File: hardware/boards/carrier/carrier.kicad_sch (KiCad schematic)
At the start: 43 parts, among them J1 XT30PW(2+2)-M.G.B_SLOT, Q1 IPB020N10N5LF, Q2 2N7002, Q3 2N7002, U2 LM5163DDAR, U3 LMX5069MS, U4 INA237AIDGSR

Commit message: hardware: standardize carrier schematic presentation
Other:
- sheet STM32 Housekeeping and Status ports: added none; removed +3V3, GND

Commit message: checkpoint: carrier schematic refinements
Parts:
- C1: value 1uF 100V X7R -> 1uF 100V
- C2: value 680nF 10% X7R -> 680nF
- J1: value XT30PW(2+2)-M.G.B_SLOT -> XT30PW(2+2)
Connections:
- net VIN_RAW: no longer J1.1 (Pin_1)
- new net VCC: J1.1 (Pin_1)
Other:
- moved on the sheet: C10, R18, R8

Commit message: hardware: split carrier power controls and adopt SMBus
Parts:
- removed C1: 1uF 100V, Capacitor_SMD:C_1206_3216Metric, symbol Device:C
- removed C10: 100nF diff, Capacitor_SMD:C_0603_1608Metric, symbol Device:C
- removed C2: 680nF, Capacitor_SMD:C_0603_1608Metric, symbol Device:C
- removed D1: SMCJ48A, Diode_SMD:D_SMC, symbol Device:D_Zener
- removed MOD1: SW3538_140W_Module, mini-rack-power:SW3538_140W_Module, symbol mini-rack-power:SW3538_140W_Module
- removed Q1: IPB020N10N5LF, Package_TO_SOT_SMD:TO-263-3_TabPin2, symbol Transistor_FET:Q_NMOS_GDS
- removed Q2, Q3: 2N7002, Package_TO_SOT_SMD:SOT-23, symbol Transistor_FET:2N7002
- removed R1: 6mR 1% 3W, Resistor_SMD:R_2512_6332Metric, symbol Device:R
- removed R10: 100k, Resistor_SMD:R_0603_1608Metric, symbol Device:R
- removed R11, R19: 10k, Resistor_SMD:R_0603_1608Metric, symbol Device:R
- removed R17, R18: 10R, Resistor_SMD:R_0603_1608Metric, symbol Device:R
- removed R2: 100R, Resistor_SMD:R_0603_1608Metric, symbol Device:R
- removed R20: 0R A0=0, Resistor_SMD:R_0603_1608Metric, symbol Device:R
- removed R21: 0R A0=1 DNP, Resistor_SMD:R_0603_1608Metric, symbol Device:R
- removed R22: 0R A1=0, Resistor_SMD:R_0603_1608Metric, symbol Device:R
- removed R23: 0R A1=1 DNP, Resistor_SMD:R_0603_1608Metric, symbol Device:R
- removed R3: 36.0k 1%, Resistor_SMD:R_0603_1608Metric, symbol Device:R
- removed R4: 110k 1% UVLO, Resistor_SMD:R_0603_1608Metric, symbol Device:R
- removed R5: 18k 1% UVLO, Resistor_SMD:R_0603_1608Metric, symbol Device:R
- removed R6: 110k 1% OVLO, Resistor_SMD:R_0603_1608Metric, symbol Device:R
- removed R7: 5.1k 1% OVLO, Resistor_SMD:R_0603_1608Metric, symbol Device:R
- removed R8: 110k 1%, Resistor_SMD:R_0603_1608Metric, symbol Device:R
- removed R9: 36k 1%, Resistor_SMD:R_0603_1608Metric, symbol Device:R
- removed U3: LMX5069MS, Package_SO:MSOP-10_3x3mm_P0.5mm, symbol Power_Management:LM5069MM-2
- removed U4: INA237AIDGSR, Package_SO:TSSOP-10_3x3mm_P0.5mm, symbol Sensor_Energy:INA237
- C3, C4: value 2.2uF 100V X7R -> 2.2uF 100V
- C5: value 2.2nF 50V X7R -> 2.2nF 50V
- C6: value 2.2nF X7R -> 2.2nF
- C7: value 220pF C0G -> 220pF
- C8: value 22uF 25V X7R -> 22uF 25V
- L1: value 68uH YNR6045-680M -> 68uH
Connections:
- net VIN_RAW is gone; now on net VCC: C3.1, C4.1, U2.2 (VIN), U2.3 (EN/UVLO)
- net UP_I2C_SCL renamed BP_SMBUS_SCL
- net UP_I2C_SDA renamed BP_SMBUS_SDA
- no-connect marks 1 -> 0
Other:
- added sheet Protected Power and Controls (01_power_control.kicad_sch)
- sheet STM32 Housekeeping and Status ports: added BP_SMBUS_SCL, BP_SMBUS_SDA; removed UP_I2C_SCL, UP_I2C_SDA
- note added: "ASSEMBLY / FOOTPRINT CHECKS L1 footprint intentionally unassigned: create/verify against the YNR6045 manufacturer land pattern. Verify U2 package pin numbering and exposed-pad requirements against manufacturer drawings."
- note added: "BACKPLANE INTERFACE + LOCAL 3.3 V SUPPLY"
- note added: "RELEASE BLOCKER - CONNECTOR POLARITY Current carrier assumption: J1 pin 1 = VCC, pin 2 = GND, pin 3 = SMBus SDA, pin 4 = SMBus SCL. Backplane-prototype presently shows the power pins oppositely. Confirm physical mated contacts and drawing viewpoints, then make symbol pins, footprint pads, net assignments, and notes consistent in every carrier/backplane project before fabrication."
- note removed: "ASSEMBLY / FOOTPRINT CHECKS L1 footprint intentionally unassigned: create/verify against the YNR6045 manufacturer land pattern. Before PCB work, verify U1/U2/U3/U4/Q1 package pin numbering and exposed-pad requirements against manufacturer drawings. R21/R23 select alternate INA237 address states and are DNP."
- note removed: "BACKPLANE INTERFACE + PROTECTED PD POWER"
- note removed: "Default OFF: R8/R9 drive Q2 on unless PA1 drives Q3. LMX5069 auto-retries; STM32 observes PD_PGOOD and may remove PD_ENABLE."
- note removed: "POWER / CURRENT MONITOR"
- note removed: "Power path: VIN_RAW -> R1 (6 mR Kelvin-routed) -> HS_SENSE -> Q1 -> PD_VIN_SW"
- note removed: "Q1 SOA RELEASE GATE Prove IPB020N10N5LF at the hot corner: approximately 66 W inferred maximum power limit and 66.5 ms maximum TIMER interval. Do not substitute Q1 using RDS(on) alone. Validate current/power limits and startup on hardware."
- note removed: "R17/R18 are Kelvin sense traces from the R1 pads. U4 VBUS intentionally measures after Q1."
- note removed: "RELEASE BLOCKER - CONNECTOR POLARITY Current carrier assumption: J1 pin 1 = VIN_RAW, pin 2 = GND, pin 3 = SDA, pin 4 = SCL. Backplane-prototype presently shows the power pins oppositely. Confirm physical mated contacts and drawing viewpoints, then make symbol pins, footprint pads, net assignments, and notes consistent in every carrier/backplane project before fabrication."
- title: USB-C PD Carrier - Protected Power and Local Supply -> USB-C PD Carrier - Backplane Interface and Local Supply

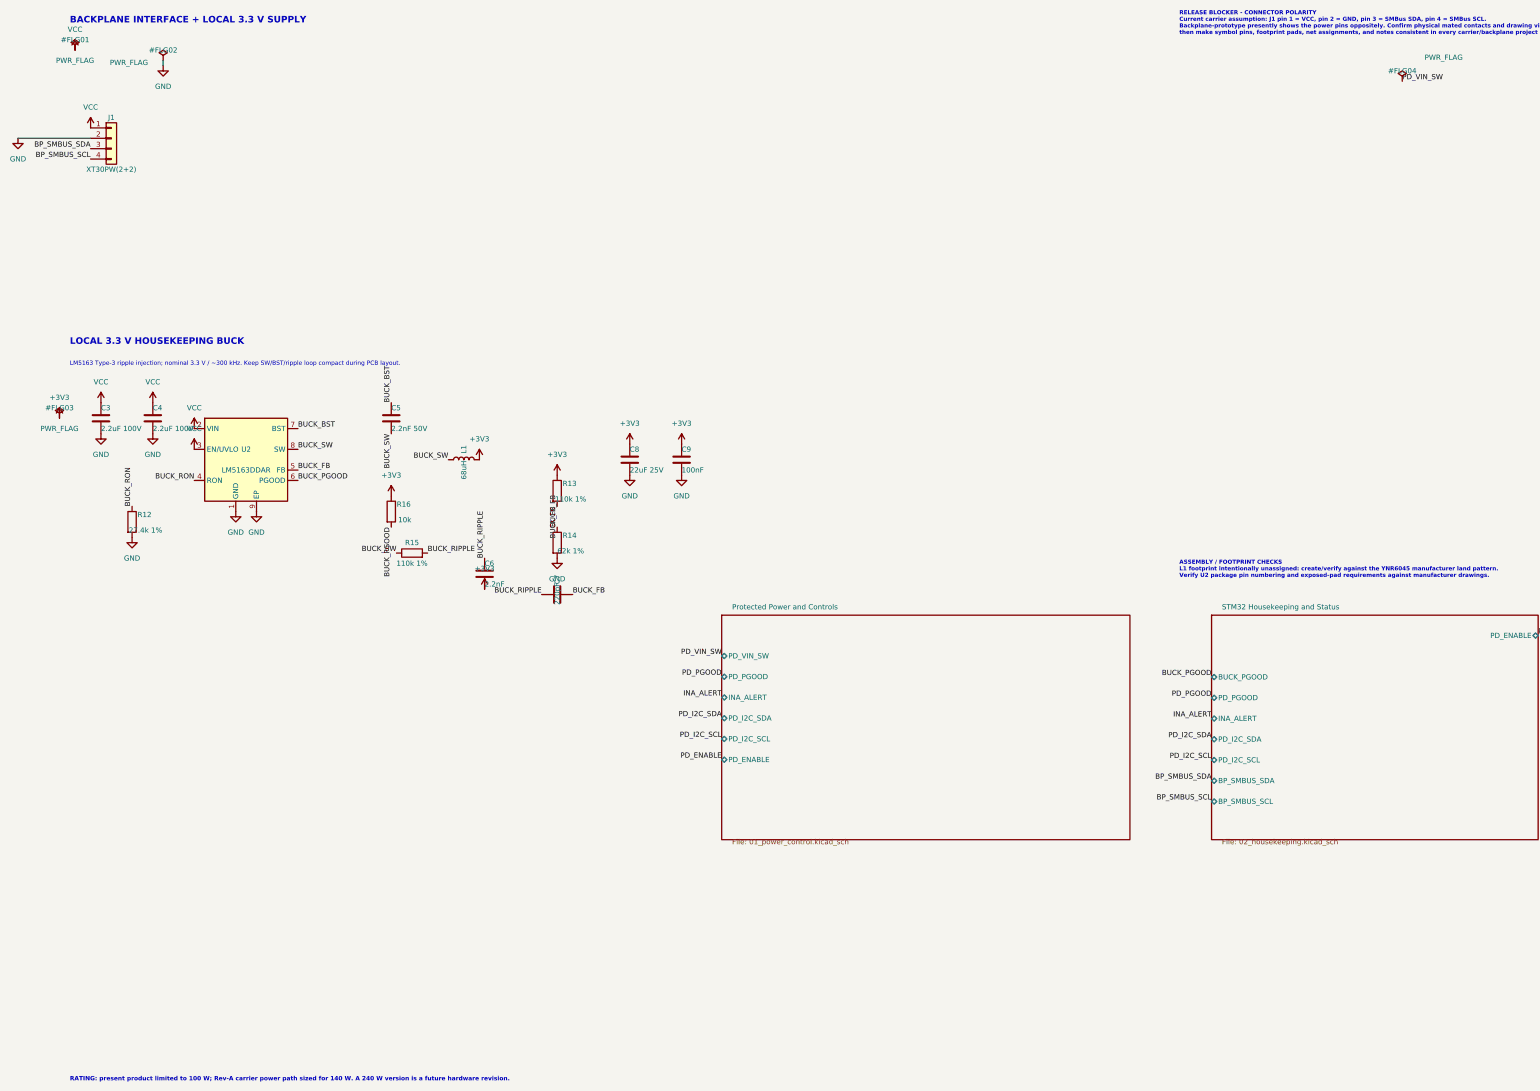
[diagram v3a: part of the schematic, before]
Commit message: checkpoint: carrier schematic edits and SW3538 references
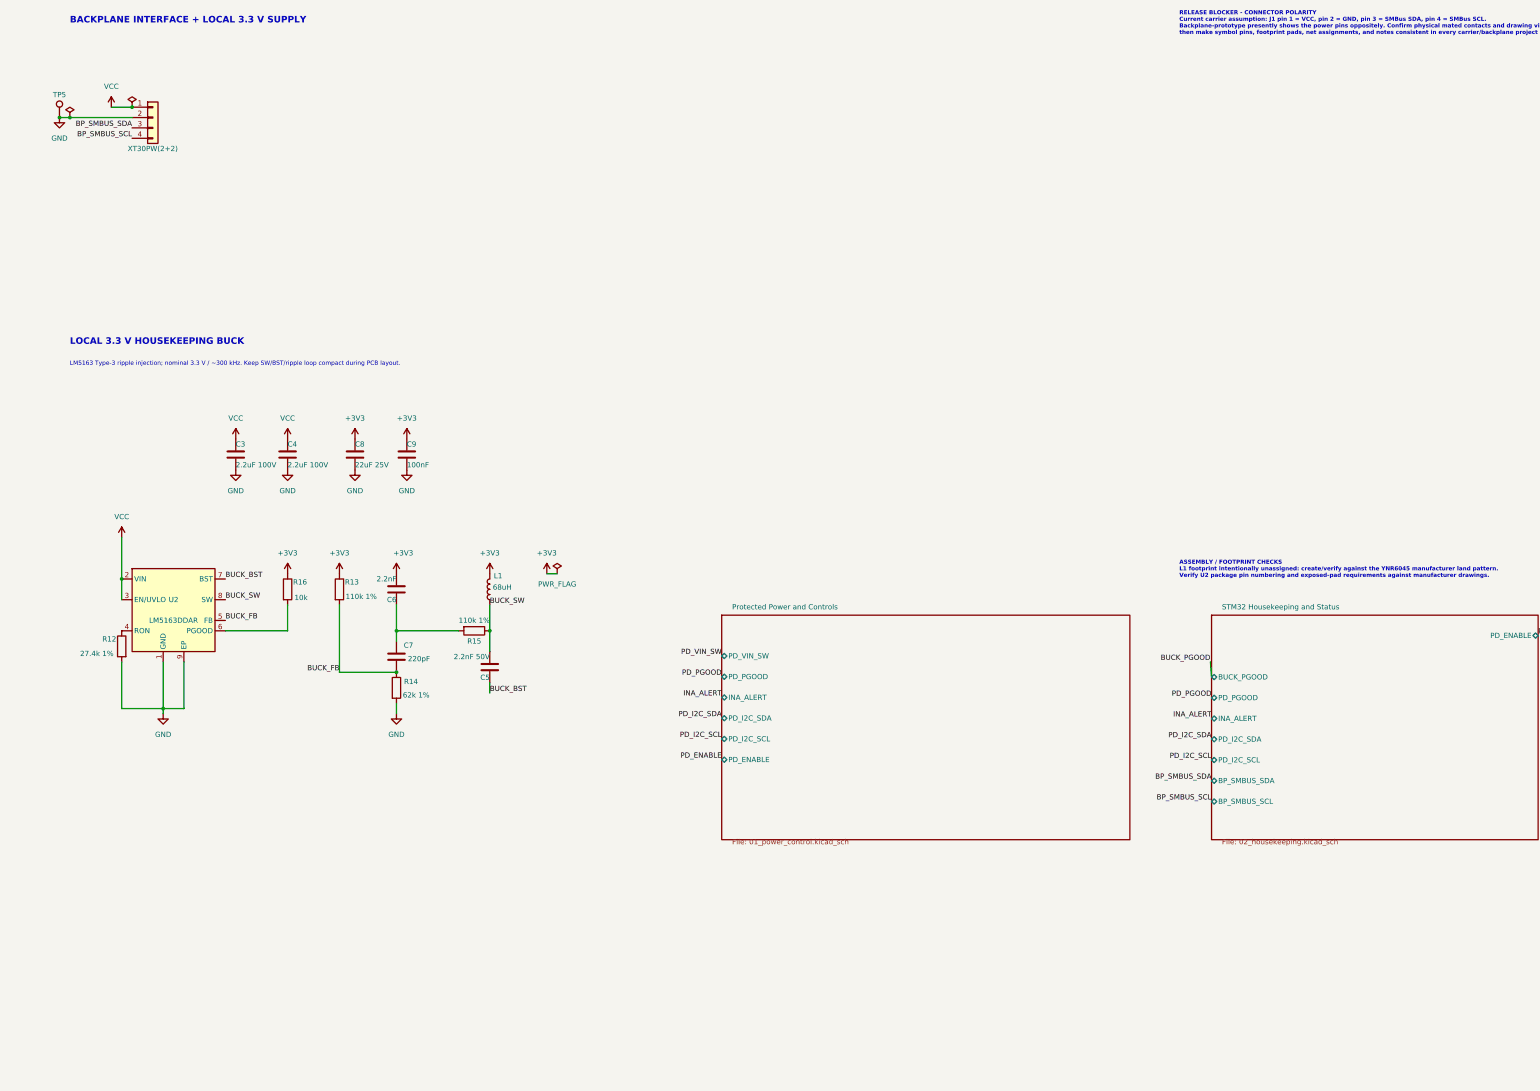
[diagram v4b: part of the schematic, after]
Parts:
- added TP5: GND, TestPoint:TestPoint_Pad_D1.0mm, symbol Connector:TestPoint
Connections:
- net BUCK_PGOOD: no longer R16.2, U2.6 (PGOOD)
- net GND: now also TP5.1
- net BUCK_RIPPLE: no longer names the net of C6.1, C7.1, R15.2
- net BUCK_RON: no longer names the net of R12.1, U2.4 (RON)
- new net: R16.2, U2.6 (PGOOD)
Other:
- note removed: "RATING: present product limited to 100 W; Rev-A carrier power path sized for 140 W. A 240 W version is a future hardware revision."
- moved on the sheet: C3, C4, C5, C6, C7, C8, C9, L1, R12, R13, R14, R15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

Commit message: hardware: route SW3538 IRQ to carrier MCU
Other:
- sheet Protected Power and Controls ports: added PD_IRQ; removed none
- sheet STM32 Housekeeping and Status ports: added PD_IRQ; removed none
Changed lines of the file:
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@@
 		)
 	)
+	(label "PD_IRQ"
+		(at 180 200.48 180)
+		(effects
+			(font
+				(size 1.27 1.27)
+			)
+			(justify right bottom)
+		)
+	)
+	(label "PD_IRQ"
+		(at 300 210.72 180)
+		(effects
+			(font
+				(size 1.27 1.27)
+			)
+			(justify right bottom)
+		)
+	)
 	(label "BUCK_FB"
 		(at 86.36 173.99 180)
@@
 			)
 		)
+		(pin "PD_IRQ" input
+			(at 300 210.72 180)
+			(effects
+				(font
+					(size 1.27 1.27)
+				)
+				(justify right)
+			)
+		)
 		(instances
 			(project "carrier"
@@
 			(effects
 				(font
+					(size 1.27 1.27)
+				)
+				(justify right)
+			)
+		)
+		(pin "PD_IRQ" output
+			(at 180 200.48 180)
+			(effects
+				(font

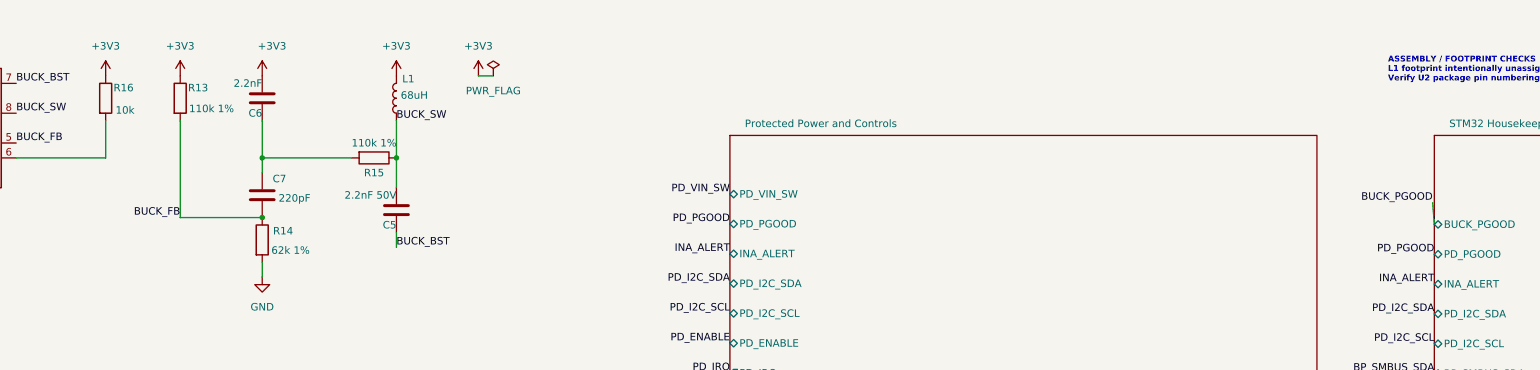
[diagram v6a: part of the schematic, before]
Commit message: hardware: fix carrier buck status and programming header
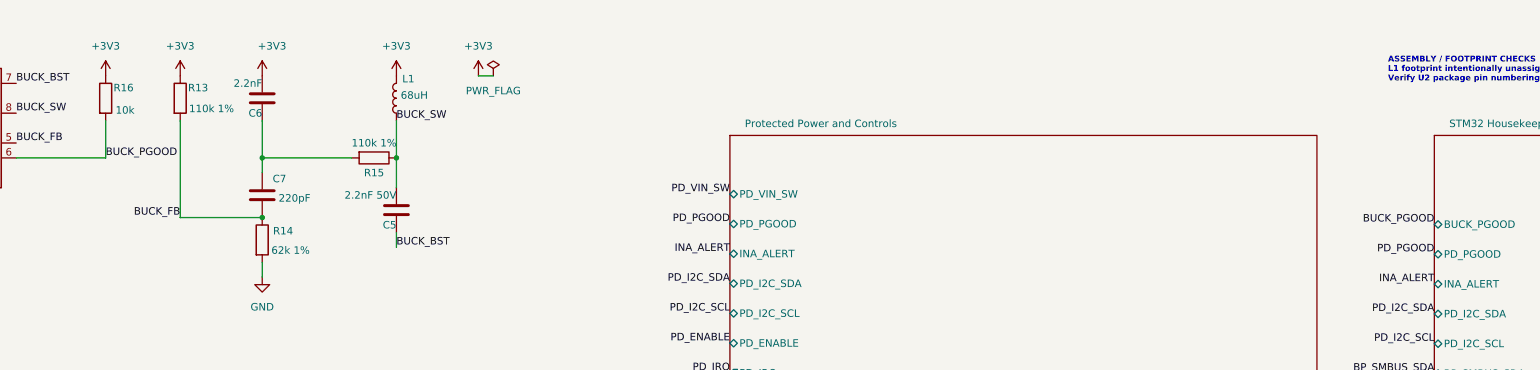
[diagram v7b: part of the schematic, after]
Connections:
- net BUCK_PGOOD: now also R16.2, U2.6 (PGOOD)
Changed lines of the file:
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@@
 		)
 	)
-	(wire
-		(pts
-			(xy 299.72 171.45) (xy 300 175.16)
-		)
-		(stroke
-			(width 0)
-			(type default)
+	(label "BUCK_PGOOD"
+		(at 73.66 163.83 0)
+		(effects
+			(font
+				(size 1.27 1.27)
+			)
+			(justify left bottom)
 		)
 	)
@@
 	)
 	(label "BUCK_PGOOD"
-		(at 299.72 171.45 180)
+		(at 300 175.16 180)
 		(effects
 			(font

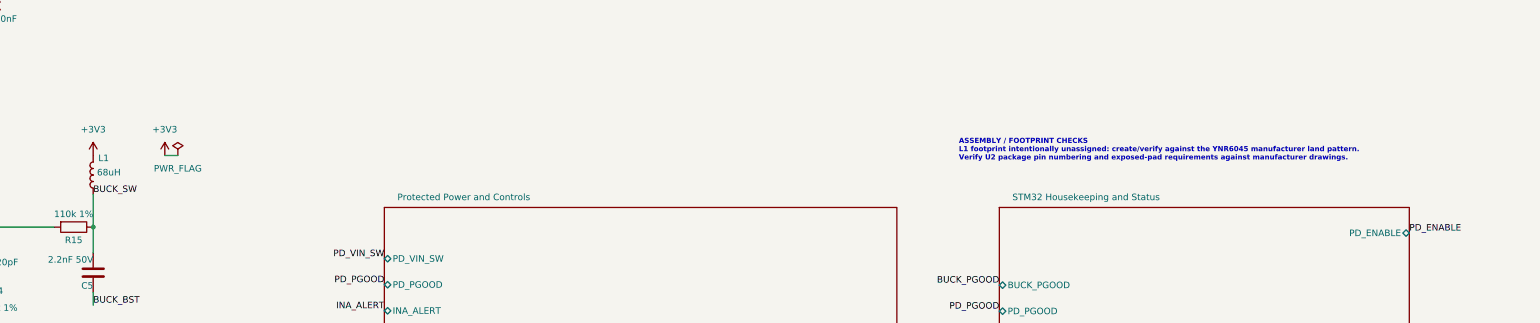
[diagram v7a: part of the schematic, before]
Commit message: hardware: select carrier buck inductor
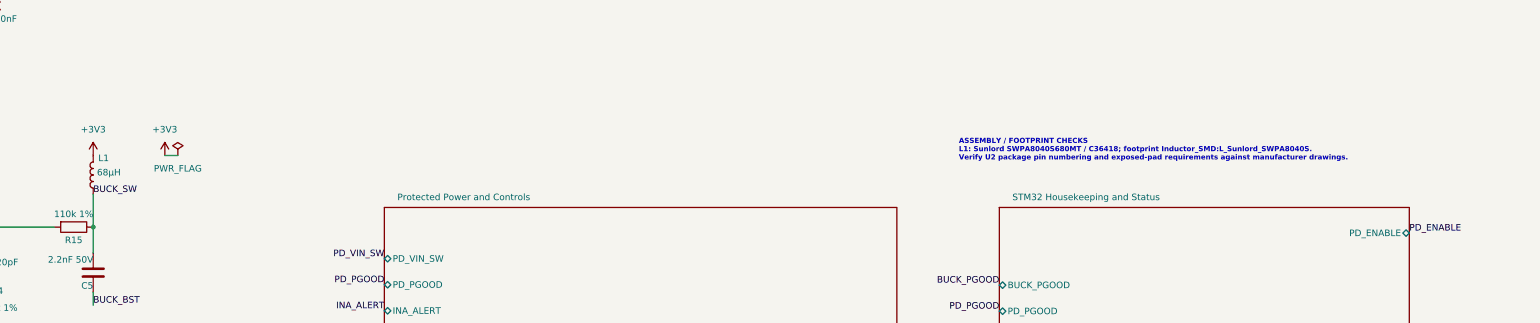
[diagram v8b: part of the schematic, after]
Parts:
- L1: value 68uH -> 68μH; footprint (none) -> Inductor_SMD:L_Sunlord_SWPA8040S; Footprint_Status UNASSIGNED - verify manufacturer land pattern -> ASSIGNED - KiCad Sunlord SWPA8040S manufacturer land pattern; LCSC C341069 -> C36418; MPN YNR6045-680M -> SWPA8040S680MT; Manufacturer YJYCOIN -> Sunlord
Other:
- note added: "ASSEMBLY / FOOTPRINT CHECKS L1: Sunlord SWPA8040S680MT / C36418; footprint Inductor_SMD:L_Sunlord_SWPA8040S. Verify U2 package pin numbering and exposed-pad requirements against manufacturer drawings."
- note removed: "ASSEMBLY / FOOTPRINT CHECKS L1 footprint intentionally unassigned: create/verify against the YNR6045 manufacturer land pattern. Verify U2 package pin numbering and exposed-pad requirements against manufacturer drawings."
